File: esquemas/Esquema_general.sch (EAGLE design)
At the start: 36 parts

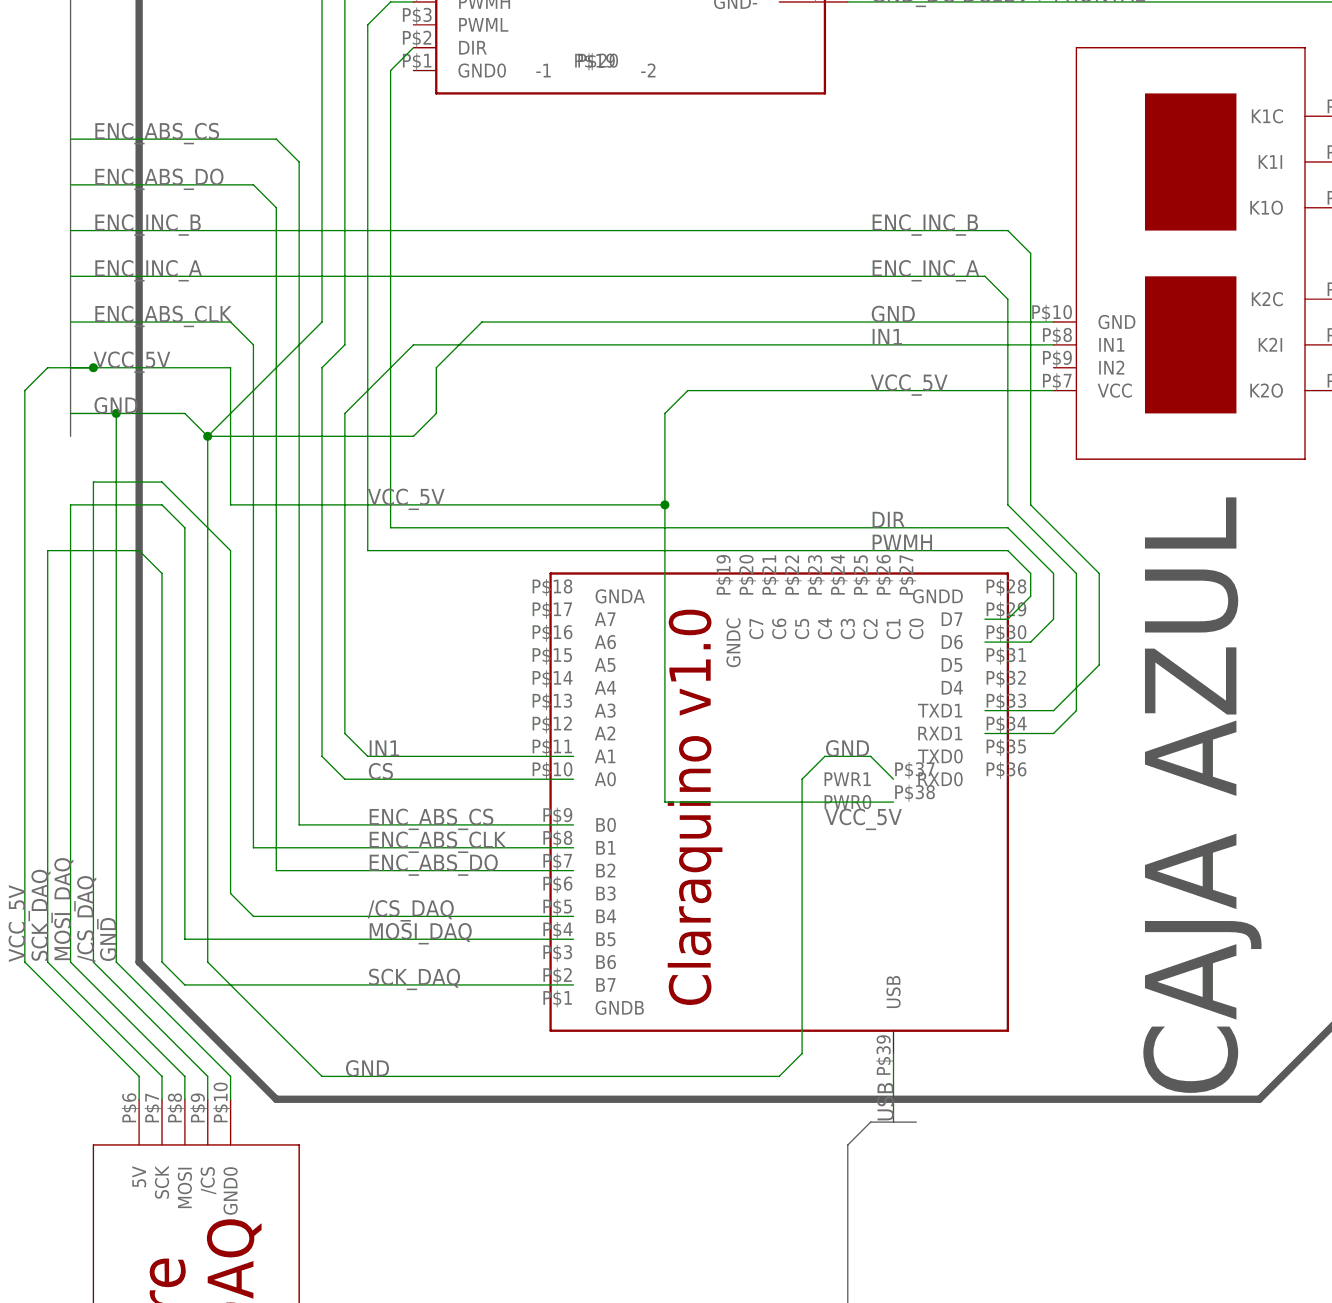
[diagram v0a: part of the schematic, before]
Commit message: Sch Lib de Claraquino, cambio de estilo:
- No mostrar nombres pines PCB (tampoco tiene sentido si no es un componente real).
- dibujar pines de forma más "estándard": con longitud en vez de puntos.
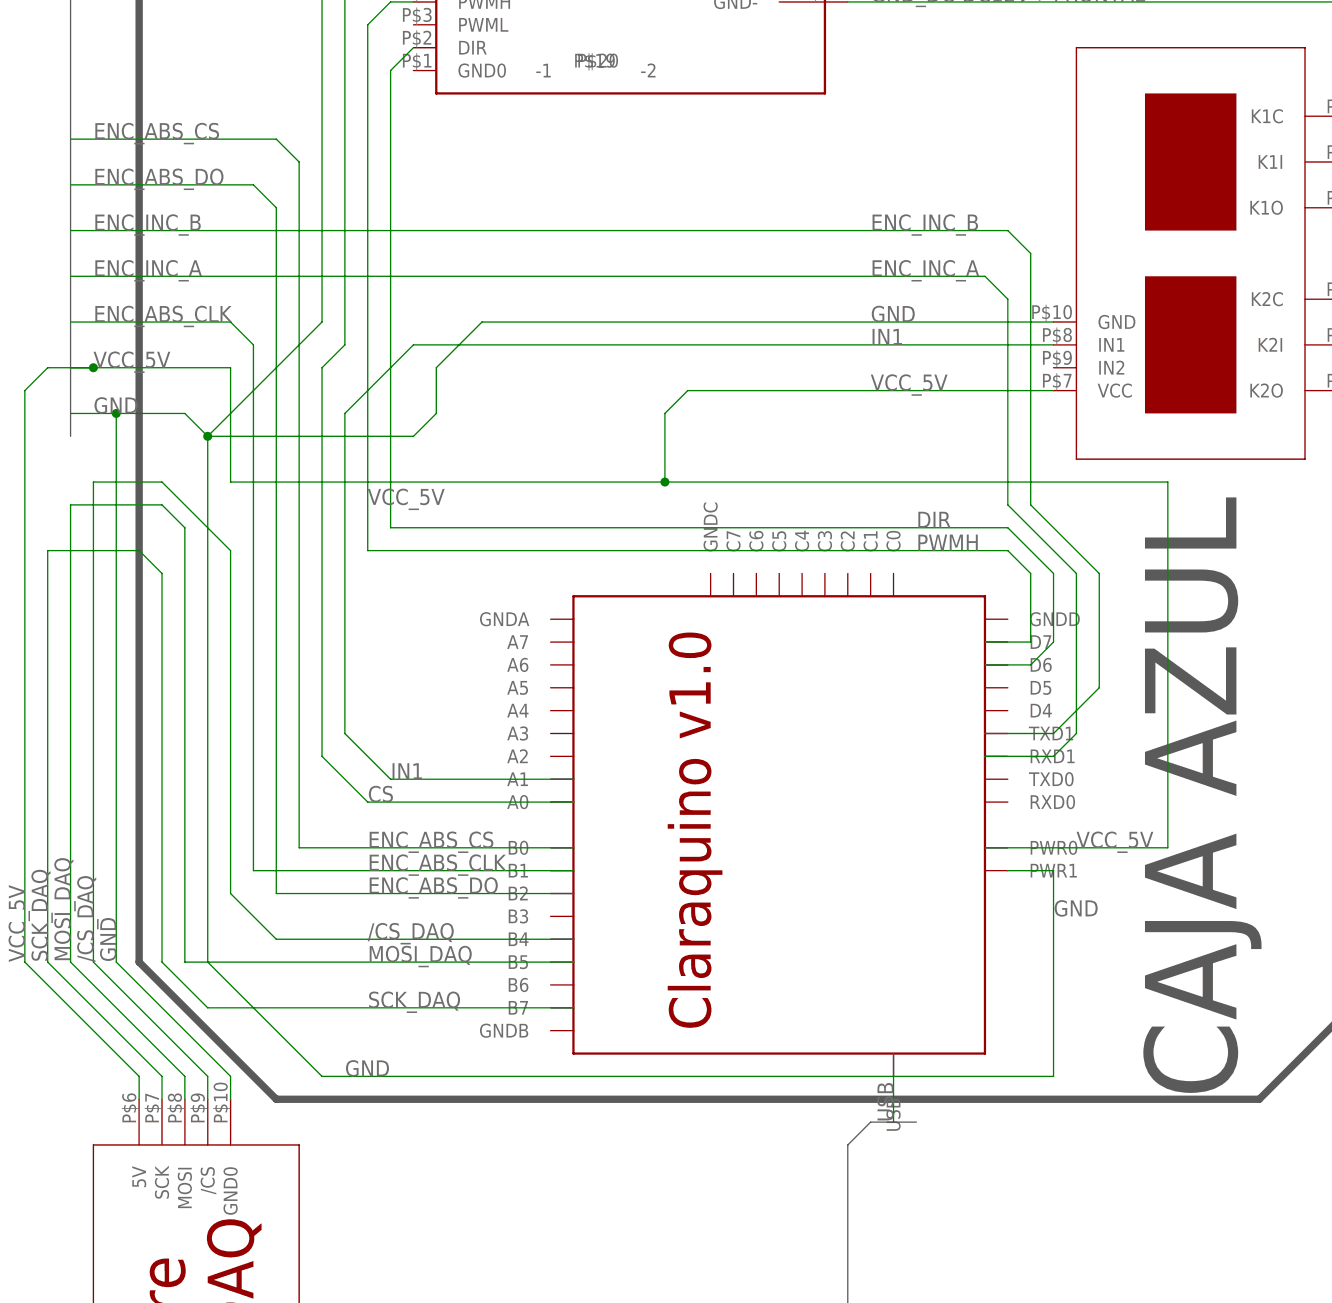
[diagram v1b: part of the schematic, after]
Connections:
- net GND: no longer U$24.PWR1
